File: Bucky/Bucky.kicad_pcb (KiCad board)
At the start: 2 copper layers, 81 x 48 mm, 29 parts, among them J1 XT60PW-M, J10 XT30AW-M, J11 XT30AW-M, J12 XT30AW-M, J13 XT30AW-M, J14 XT30AW-M, J2 XT60PW-M, J3 XT30PW-M, J4 XT30PW-M, J5 XT30PW-M, J6 XT30PW-M, J7 XT30AW-M, J8 XT30AW-M, J9 XT30AW-M

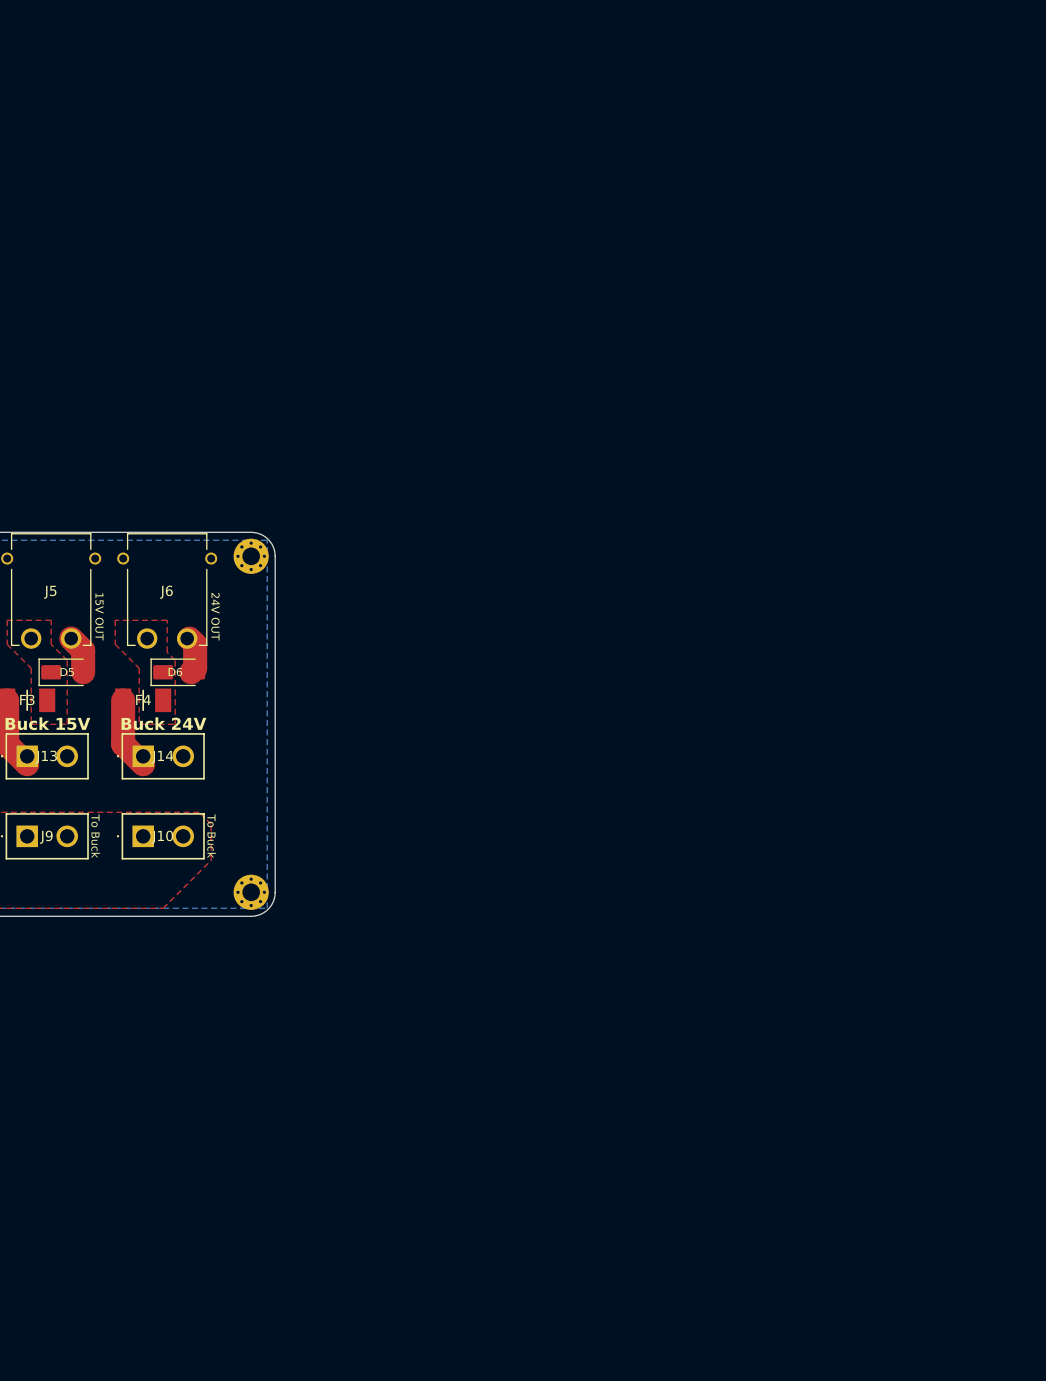
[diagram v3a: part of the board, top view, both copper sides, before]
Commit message: added features from GEODE to the schematics
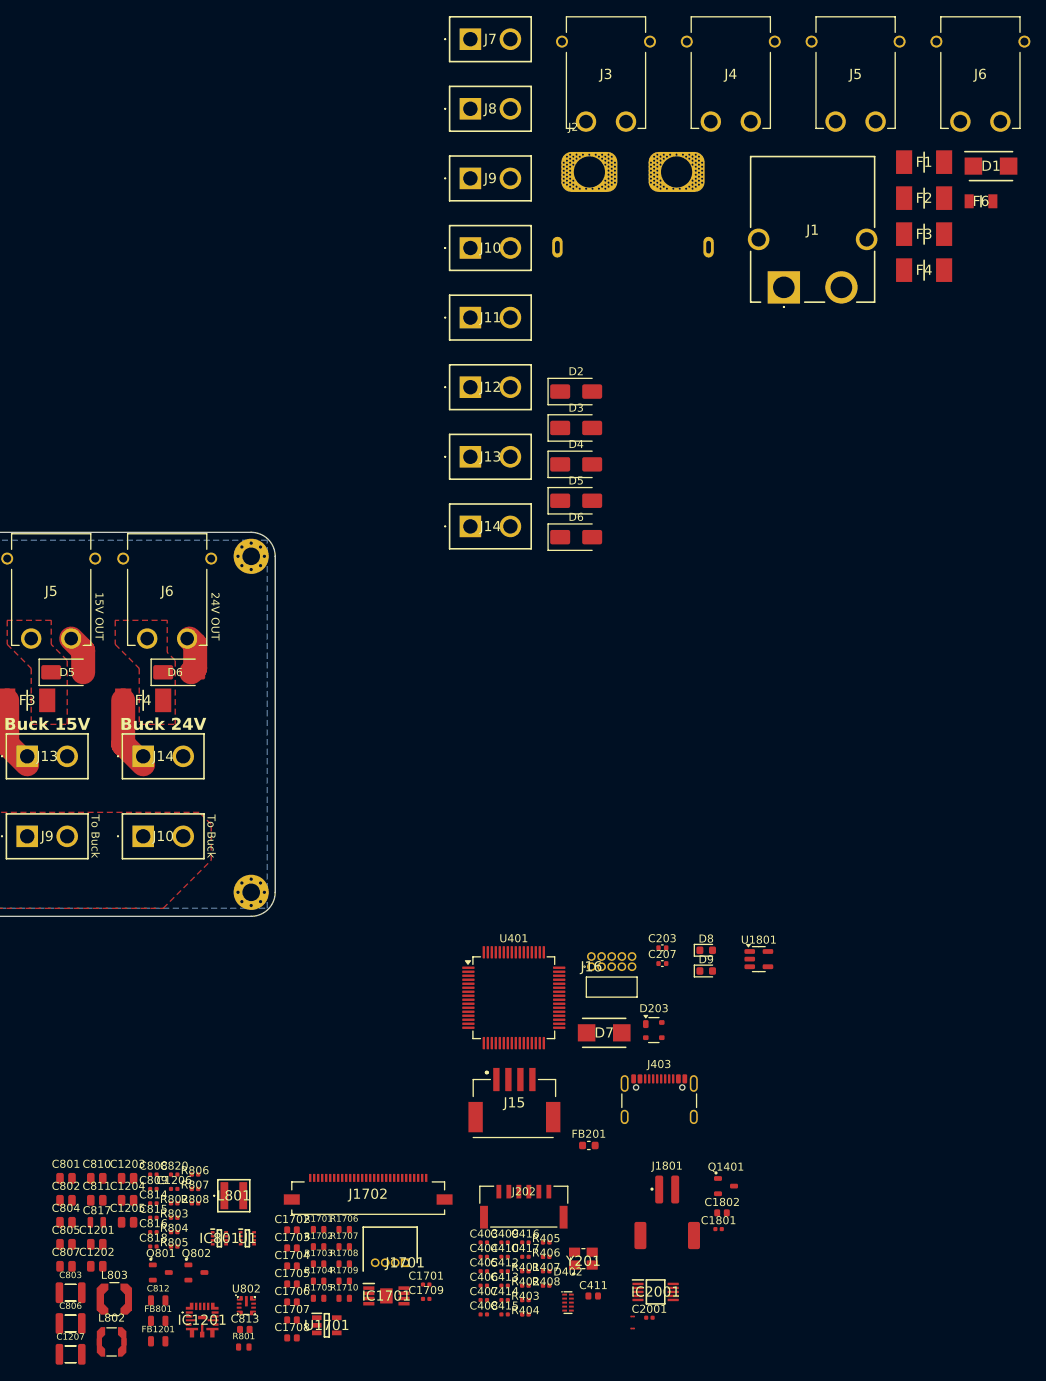
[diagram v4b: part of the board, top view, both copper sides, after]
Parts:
- added C1201: 2u2 X7R 100V, 0_capacitor_smd:C_0805_2012_DensityHigh, F.Cu at (118.7, 155.0)
- added C1202: 2u2 X7R 100V, 0_capacitor_smd:C_0805_2012_DensityHigh, F.Cu at (118.7, 157.8)
- added C1203: 2u2 X7R 100V, 0_capacitor_smd:C_0805_2012_DensityHigh, F.Cu at (122.5, 146.8)
- added C1204: 100n X7R 100V, 0_capacitor_smd:C_0805_2012_DensityHigh, F.Cu at (122.5, 149.5)
- added C1205: 2.2u X7R 25V, 0_capacitor_smd:C_0805_2012_DensityHigh, F.Cu at (122.5, 152.2)
- added C1206: 100n X7R 50V, 0_capacitor_smd:C_0402_1005_DensityHigh, F.Cu at (128.4, 148.1)
- added C1207: 10u X7R 25V, 0_capacitor_smd:C_1210_3225_DensityHigh, F.Cu at (115.4, 168.8)
- added C1701: 100n X7R 50V, 0_capacitor_smd:C_0402_1005_DensityHigh, F.Cu at (159.9, 160.0)
- added C1702: 4.7n X7R 50V, 0_capacitor_smd:C_0603_1608_DensityHigh, F.Cu at (143.1, 153.2)
- added C1703: 4.7n X7R 50V, 0_capacitor_smd:C_0603_1608_DensityHigh, F.Cu at (143.1, 155.4)
- added C1704: 4.7n X7R 50V, 0_capacitor_smd:C_0603_1608_DensityHigh, F.Cu at (143.1, 157.7)
- added C1705: 470n X5R 16V, 0_capacitor_smd:C_0603_1608_DensityHigh, F.Cu at (143.1, 159.9)
- added C1706: 470n X5R 16V, 0_capacitor_smd:C_0603_1608_DensityHigh, F.Cu at (143.1, 162.2)
- added C1707: 220n X7R 10V, 0_capacitor_smd:C_0603_1608_DensityHigh, F.Cu at (143.1, 164.4)
- added C1708: 1u X7R 16V, 0_capacitor_smd:C_0603_1608_DensityHigh, F.Cu at (143.1, 166.7)
- added C1709: 100n X7R 50V, 0_capacitor_smd:C_0402_1005_DensityHigh, F.Cu at (159.9, 161.8)
- added C1801: 100n X7R 50V, 0_capacitor_smd:C_0402_1005_DensityHigh, F.Cu at (196.4, 153.1)
- added C1802: 4.7u X7R 16V, 0_capacitor_smd:C_0603_1608_DensityHigh, F.Cu at (196.8, 151.1)
- added C2001: 100n X7R 50V, 0_capacitor_smd:C_0402_1005_DensityHigh, F.Cu at (187.8, 164.2)
- added C203: 12p NP0 25V, Capacitor_SMD:C_0402_1005Metric, F.Cu at (189.4, 117.9)
- added C207: 12p NP0 25V, Capacitor_SMD:C_0402_1005Metric, F.Cu at (189.4, 119.9)
- added C403: 100n X7R 50V, 0_capacitor_smd:C_0402_1005_DensityHigh, F.Cu at (167.1, 154.8)
- added C404: 100n X7R 50V, 0_capacitor_smd:C_0402_1005_DensityHigh, F.Cu at (167.1, 156.6)
- added C405: 100n X7R 50V, 0_capacitor_smd:C_0402_1005_DensityHigh, F.Cu at (167.1, 158.4)
- added C406: 1u X7R 10V, 0_capacitor_smd:C_0402_1005_DensityHigh, F.Cu at (167.1, 160.2)
- added C407: 100n X7R 50V, 0_capacitor_smd:C_0402_1005_DensityHigh, F.Cu at (167.1, 162.0)
- added C408: 100n X7R 50V, 0_capacitor_smd:C_0402_1005_DensityHigh, F.Cu at (167.1, 163.8)
- added C409: 100n X7R 50V, 0_capacitor_smd:C_0402_1005_DensityHigh, F.Cu at (169.7, 154.8)
- added C410: 100n X7R 50V, 0_capacitor_smd:C_0402_1005_DensityHigh, F.Cu at (169.7, 156.6)
- added C411: 4u7 X7R 16V, 0_capacitor_smd:C_0603_1608_DensityHigh, F.Cu at (180.8, 161.5)
- added C412: 1u X7R 10V, 0_capacitor_smd:C_0402_1005_DensityHigh, F.Cu at (169.7, 158.4)
- added C413: 1u X7R 10V, 0_capacitor_smd:C_0402_1005_DensityHigh, F.Cu at (169.7, 160.2)
- added C414: 100n X7R 50V, 0_capacitor_smd:C_0402_1005_DensityHigh, F.Cu at (169.7, 162.0)
- added C415: 1u X7R 10V, 0_capacitor_smd:C_0402_1005_DensityHigh, F.Cu at (169.7, 163.8)
- added C416: 100n X7R 50V, 0_capacitor_smd:C_0402_1005_DensityHigh, F.Cu at (172.3, 154.8)
- added C417: 100n X7R 50V, 0_capacitor_smd:C_0402_1005_DensityHigh, F.Cu at (172.3, 156.6)
- added C801: 2u2 X7R 100V, 0_capacitor_smd:C_0805_2012_DensityHigh, F.Cu at (114.8, 146.8)
- added C802: 100n X7R 100V, 0_capacitor_smd:C_0805_2012_DensityHigh, F.Cu at (114.8, 149.5)
- added C803: 10u X7R 25V, 0_capacitor_smd:C_1210_3225_DensityHigh, F.Cu at (115.4, 161.1)
- added C804: 2.2u X7R 25V, 0_capacitor_smd:C_0805_2012_DensityHigh, F.Cu at (114.8, 152.2)
- added C805: 2.2u X7R 25V, 0_capacitor_smd:C_0805_2012_DensityHigh, F.Cu at (114.8, 155.0)
- added C806: 4.7uF X7R 25V, 0_capacitor_smd:C_1210_3225_DensityHigh, F.Cu at (115.4, 164.9)
- added C807: 22u X7R 10V, 0_capacitor_smd:C_0805_2012_DensityHigh, F.Cu at (114.8, 157.8)
- added C808: 100n X7R 50V, 0_capacitor_smd:C_0402_1005_DensityHigh, F.Cu at (125.8, 146.3)
- added C809: 100n X7R 50V, 0_capacitor_smd:C_0402_1005_DensityHigh, F.Cu at (125.8, 148.1)
- added C810: 2u2 X7R 100V, 0_capacitor_smd:C_0805_2012_DensityHigh, F.Cu at (118.7, 146.8)
- added C811: 2u2 X7R 100V, 0_capacitor_smd:C_0805_2012_DensityHigh, F.Cu at (118.7, 149.5)
- added C812: 2u2 X7R 100V, 0_resistor_smd:R_0805_2012_DensityHigh, F.Cu at (126.4, 162.0)
- added C813: 100n X7R 100V, 0_capacitor_smd:C_0603_1608_DensityHigh, F.Cu at (137.2, 165.6)
- added C814: 1u X7R 10V, 0_capacitor_smd:C_0402_1005_DensityHigh, F.Cu at (125.8, 149.9)
- added C815: 100n X7R 50V, 0_capacitor_smd:C_0402_1005_DensityHigh, F.Cu at (125.8, 151.7)
- added C816: 100n X7R 50V, 0_capacitor_smd:C_0402_1005_DensityHigh, F.Cu at (125.8, 153.5)
- added C817: 22u X7R 10V, 0_capacitor_smd:C_0805_2012_DensityHighest, F.Cu at (118.7, 152.2)
- added C818: 1u X7R 10V, 0_capacitor_smd:C_0402_1005_DensityHigh, F.Cu at (125.8, 155.3)
- added C820: 1u X7R 10V, 0_capacitor_smd:C_0402_1005_DensityHigh, F.Cu at (128.4, 146.3)
- added D1: SMBJ51CD-M3_H, SamacSys_Parts:DIOM5436X244N, F.Cu at (230.5, 20.2)
- added D2: SMAJ24A, Diode_SMD:D_SMA, F.Cu at (178.6, 48.4)
- added D203: PRTR5V0U2X, Package_TO_SOT_SMD:SOT-143, F.Cu at (188.3, 128.2)
- added D3: SMAJ5.0A, Diode_SMD:D_SMA, F.Cu at (178.6, 53.0)
- added D4: SMAJ12A, Diode_SMD:D_SMA, F.Cu at (178.6, 57.5)
- added D402: PESD4USB3U-TBSX, 0_package_DFN_QFN:SOT1176D, F.Cu at (177.6, 162.3)
- added D5: SMAJ15A, Diode_SMD:D_SMA, F.Cu at (178.6, 62.1)
- added D6: SMAJ24A, Diode_SMD:D_SMA, F.Cu at (178.6, 66.6)
- added D7: SMBJ3V3-M3_5B, SamacSys_Parts:DIONM5436X244N, F.Cu at (182.1, 128.6)
- added D8: GREEN, LED_SMD:LED_0603_1608Metric, F.Cu at (194.9, 118.2)
- added D9: GREEN, LED_SMD:LED_0603_1608Metric, F.Cu at (194.9, 120.8)
- added F1: 0451015.MRL, SamacSys_Parts:FUSC6127X294N, F.Cu at (222.1, 19.7)
- added F2: 0451015.MRL, SamacSys_Parts:FUSC6127X294N, F.Cu at (222.1, 24.2)
- added F3: 0451015.MRL, SamacSys_Parts:FUSC6127X294N, F.Cu at (222.1, 28.7)
- added F4: 0451015.MRL, SamacSys_Parts:FUSC6127X294N, F.Cu at (222.1, 33.2)
- added F6: 0806040.WR, SamacSys_Parts:FUSC3216X110N, F.Cu at (229.2, 24.6)
- added FB1201: 1k @ 100MHz, 0_resistor_smd:R_0805_2012_DensityHigh, F.Cu at (126.4, 167.1)
- added FB201: 100R@100MHz, Inductor_SMD:L_0603_1608Metric, F.Cu at (180.2, 142.6)
- added FB801: 1k @ 100MHz, 0_resistor_smd:R_0805_2012_DensityHigh, F.Cu at (126.4, 164.6)
- added IC1201: MAX25262AFOF_VY+, 0_switching_regulator:MAX25262AFOFVY, F.Cu at (131.9, 164.5)
- added IC1701: TPA6205A1DGN, 0_connectors:SOP65P490X110-9N, F.Cu at (154.9, 161.4)
- added IC2001: INA239AQDGSRQ1, 0_diode_smd:SOP50P490X110-10N, F.Cu at (188.6, 160.9)
- added IC801: TPS629206QDRLRQ1, 0_switching_regulator:SOTFL50P160X60-8N, F.Cu at (134.0, 154.2)
- added J1: XT60PW-M, SamacSys_Parts:XT60PWM, F.Cu at (204.6, 35.4)
- added J10: XT30AW-M, SamacSys_Parts:XT30AWM, F.Cu at (165.4, 30.5)
- added J11: XT30AW-M, SamacSys_Parts:XT30AWM, F.Cu at (165.4, 39.2)
- added J12: XT30AW-M, SamacSys_Parts:XT30AWM, F.Cu at (165.4, 47.9)
- added J13: XT30AW-M, SamacSys_Parts:XT30AWM, F.Cu at (165.4, 56.6)
- added J14: XT30AW-M, SamacSys_Parts:XT30AWM, F.Cu at (165.4, 65.3)
- added J15: 502585-0470, SamacSys_Parts:5025850470, F.Cu at (170.9, 138.0)
- added J16: FTSH-105-01-F-D-RA-K, SamacSys_Parts:FTSH-105-XX-YYY-D-RA-K, F.Cu at (180.5, 120.3)
- added J1701: 53048-0450, 0_connectors:SHDRRA4W35P0X125_1X4_675X550X350P, F.Cu at (157.2, 157.3)
- added J1702: 505110-3091, 0_connectors:5051103091, F.Cu at (152.6, 148.7)
- added J1801: S2B-PH-SM4-TB, 0_connectors:JST_PH_S2B-PH-SM4-TB_1x02-1MP_P2.00mm_Horizontal, F.Cu at (190.0, 151.0)
- added J2: XT90PW-M, 0_connectors:AMASS_XT90PW-M, F.Cu at (185.7, 30.4)
- added J202: Conn_Picoblade_JST_DEBUG, 0_connectors:CONN_SM06B-GHS-TB_JST, F.Cu at (172.1, 150.3)
- added J3: XT30PW-M, SamacSys_Parts:XT30PWM, F.Cu at (182.3, 8.75)
- added J4: XT30PW-M, SamacSys_Parts:XT30PWM, F.Cu at (197.9, 8.75)
- added J403: USB4105-GF-A, Connector_USB:USB_C_Receptacle_GCT_USB4105-xx-A_16P_TopMnt_Horizontal, F.Cu at (189.0, 138.0)
- added J5: XT30PW-M, SamacSys_Parts:XT30PWM, F.Cu at (213.6, 8.75)
- added J6: XT30PW-M, SamacSys_Parts:XT30PWM, F.Cu at (229.2, 8.75)
- added J7: XT30AW-M, SamacSys_Parts:XT30AWM, F.Cu at (165.4, 4.36)
- added J8: XT30AW-M, SamacSys_Parts:XT30AWM, F.Cu at (165.4, 13.1)
- added J9: XT30AW-M, SamacSys_Parts:XT30AWM, F.Cu at (165.4, 21.8)
- added L801: 6u8, 0_inductor_smd:XEL4030682MEC, F.Cu at (135.8, 148.9)
- added L802: 2u2, 0_inductor_smd:L_Coilcraft_LPS3314, F.Cu at (120.5, 167.2)
- added L803: 22u, 0_inductor_smd:L_Coilcraft_LPS4018, F.Cu at (120.9, 161.8)
- added NT1601: NetTieShuntH, 0_net_tie:NetTie-2_SMD_Pad0.2mm, F.Cu at (185.7, 164.0)
- added NT1602: NetTieShuntL, 0_net_tie:NetTie-2_SMD_Pad0.2mm, F.Cu at (185.7, 165.5)
- added Q1401: PMV90ENER, 0_package_SOT_TO_SMD:SOT-23-3, F.Cu at (197.3, 147.7)
- added Q801: PMV90ENER, 0_package_SOT_TO_SMD:SOT-23-3, F.Cu at (126.7, 158.5)
- added Q802: PMV90ENER, 0_package_SOT_TO_SMD:SOT-23-3, F.Cu at (131.2, 158.5)
- added R1701: 33 1% 1/10W, 0_resistor_smd:R_0603_1608_DensityHigh, F.Cu at (146.4, 153.2)
- added R1702: 33 1% 1/10W, 0_resistor_smd:R_0603_1608_DensityHigh, F.Cu at (146.4, 155.3)
- added R1703: 1k 1% 1/10W, 0_resistor_smd:R_0603_1608_DensityHigh, F.Cu at (146.4, 157.4)
- added R1704: 1k 1% 1/10W, 0_resistor_smd:R_0603_1608_DensityHigh, F.Cu at (146.4, 159.6)
- added R1705: 47k 1% 1/10W, 0_resistor_smd:R_0603_1608_DensityHigh, F.Cu at (146.4, 161.8)
- added R1706: 1k 1% 1/10W, 0_resistor_smd:R_0603_1608_DensityHigh, F.Cu at (149.6, 153.2)
- added R1707: 10k 1% 1/10W, 0_resistor_smd:R_0603_1608_DensityHigh, F.Cu at (149.6, 155.3)
- added R1708: 10k 1% 1/10W, 0_resistor_smd:R_0603_1608_DensityHigh, F.Cu at (149.6, 157.4)
- added R1709: 20k 1% 1/10W, 0_resistor_smd:R_0603_1608_DensityHigh, F.Cu at (149.6, 159.6)
- added R1710: 20k 1% 1/10W, 0_resistor_smd:R_0603_1608_DensityHigh, F.Cu at (149.6, 161.8)
- added R401: 33k 1% 1/16W, 0_resistor_smd:R_0402_1005_DensityHigh, F.Cu at (172.3, 158.4)
- added R402: 5.1k 1% 1/16W, 0_resistor_smd:R_0402_1005_DensityHigh, F.Cu at (172.3, 160.2)
- added R403: 5.1k 1% 1/16W, 0_resistor_smd:R_0402_1005_DensityHigh, F.Cu at (172.3, 162.0)
- added R404: 10k 1% 1/16W, 0_resistor_smd:R_0402_1005_DensityHigh, F.Cu at (172.3, 163.8)
- added R405: 10k 1% 1/16W, 0_resistor_smd:R_0402_1005_DensityHigh, F.Cu at (174.9, 154.8)
- added R406: 10k 1% 1/16W, 0_resistor_smd:R_0402_1005_DensityHigh, F.Cu at (174.9, 156.6)
- added R407: 27R 1% 1/5W, 0_resistor_smd:R_0402_1005_DensityHigh, F.Cu at (174.9, 158.4)
- added R408: 27R 1% 1/5W, 0_resistor_smd:R_0402_1005_DensityHigh, F.Cu at (174.9, 160.2)
- added R801: 34k 1% 1/4W, 0_resistor_smd:R_0603_1608_DensityHigh, F.Cu at (137.1, 167.8)
- added R802: 0R, 0_resistor_smd:R_0402_1005_DensityHigh, F.Cu at (128.4, 149.9)
- added R803: 10k 1%, 0_resistor_smd:R_0402_1005_DensityHigh, F.Cu at (128.4, 151.7)
- added R804: 10.7k, 0_resistor_smd:R_0402_1005_DensityHigh, F.Cu at (128.4, 153.5)
- added R805: 37k, 0_resistor_smd:R_0402_1005_DensityHigh, F.Cu at (128.4, 155.3)
- added R806: 10k 1%, 0_resistor_smd:R_0402_1005_DensityHigh, F.Cu at (131.0, 146.3)
- added R807: 470R 1% 1/8W, 0_resistor_smd:R_0402_1005_DensityHigh, F.Cu at (131.0, 148.1)
- added R808: 470R 1% 1/8W, 0_resistor_smd:R_0402_1005_DensityHigh, F.Cu at (131.0, 149.9)
- added U1: TPS2116DRLR, 0_switching_regulator:SOTFL50P160X60-8N, F.Cu at (137.5, 154.2)
- added U1701: 74LVC1G125, 0_package_SON:SOT95P280X145-5N, F.Cu at (147.4, 165.1)
- added U1801: DGD0216WT-7, Package_TO_SOT_SMD:TSOT-23-5, F.Cu at (201.5, 119.3)
- added U401: STM32G483RET6, Package_QFP:LQFP-64_10x10mm_P0.5mm, F.Cu at (170.8, 124.2)
- added U802: LMR36506MSC5RPERQ1, 0_switching_regulator:LMR36503, F.Cu at (137.4, 162.7)
- added Y201: ABM8W-48.0000MHZ-4-D1X-T3, 0_diode_smd:ABM8W480000MHZ6D1XT3, F.Cu at (179.5, 157.1)

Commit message: adapted schematics and added more protection from GEODE (Reverse Current)
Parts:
- removed the D1 at (69.0, 69.0)
- removed the D2 at (73.0, 111.0)
- removed D3 (x2): SMAJ5.0A, Diode_SMD:D_SMA
- removed D4 (x2): SMAJ12A, Diode_SMD:D_SMA
- removed D5 (x2): SMAJ15A, Diode_SMD:D_SMA
- removed D6 (x2): SMAJ24A, Diode_SMD:D_SMA
- removed the F1 at (82.0, 87.0)
- removed the F2 at (96.0, 87.0)
- removed the F3 at (110.0, 87.0)
- removed the F4 at (124.5, 87.0)
- removed the F6 at (75.5, 88.5)
- removed H1, H2, H3, H501: M2 (3.2mm), MountingHole:MountingHole_2.2mm_M2_Pad_Via
- removed the J1 at (71.0, 84.6)
- removed J10 (x2), J9 (x2): XT30AW-M, SamacSys_Parts:XT30AWM
- removed the J11 at (81.0, 94.0)
- removed the J12 at (95.5, 94.0)
- removed the J13 at (110.0, 94.0)
- removed the J14 at (124.5, 94.0)
- removed the J2 at (71.0, 102.6)
- removed the J2 at (185.7, 30.4)
- removed the J3 at (84.0, 73.4)
- removed the J4 at (98.5, 73.4)
- removed the J5 at (113.0, 73.4)
- removed the J6 at (127.5, 73.4)
- removed the J7 at (95.5, 104.0)
- removed the J7 at (165.4, 4.36)
- removed the J8 at (165.4, 13.1)
- removed the J8 at (81.0, 104.0)
- added C1: 100n X7R 50V, 0_capacitor_smd:C_0402_1005_DensityHigh, F.Cu at (98.7, 31.0)
- added C1801: 100n X7R 50V, 0_capacitor_smd:C_0402_1005_DensityHigh, F.Cu at (242.1, 84.5)
- added C1802: 4.7u X7R 16V, 0_capacitor_smd:C_0603_1608_DensityHigh, F.Cu at (238.3, 84.2)
- added C2: 100n X7R 50V, 0_capacitor_smd:C_0402_1005_DensityHigh, F.Cu at (98.7, 32.8)
- added C3: 100n X7R 50V, 0_capacitor_smd:C_0402_1005_DensityHigh, F.Cu at (98.7, 34.6)
- added C4: 10n X7R 100V, 0_capacitor_smd:C_0402_1005_DensityHigh, F.Cu at (186.1, 30.9)
- added C5: 10n X7R 100V, 0_capacitor_smd:C_0402_1005_DensityHigh, F.Cu at (186.1, 32.7)
- added C6: 100n X7R 50V, 0_capacitor_smd:C_0402_1005_DensityHigh, F.Cu at (186.1, 34.5)
- added C7: 100n X7R 50V, 0_capacitor_smd:C_0402_1005_DensityHigh, F.Cu at (186.1, 36.3)
- added C701: 10n X7R 100V, 0_capacitor_smd:C_0402_1005_DensityHigh, F.Cu at (186.1, 38.1)
- added C702: 10n X7R 100V, 0_capacitor_smd:C_0402_1005_DensityHigh, F.Cu at (186.1, 39.9)
- added C703: 100n X7R 50V, 0_capacitor_smd:C_0402_1005_DensityHigh, F.Cu at (186.1, 41.7)
- added C704: 100n X7R 50V, 0_capacitor_smd:C_0402_1005_DensityHigh, F.Cu at (186.1, 43.5)
- added D11: SMAJ15A, Diode_SMD:D_SMA, F.Cu at (90.0, 31.4)
- added D13: SMAJ24A, Diode_SMD:D_SMA, F.Cu at (90.0, 35.9)
- added D702: SMAJ5A, Diode_SMD:D_SMA, F.Cu at (90.0, 40.5)
- added D704: SMAJ12A, Diode_SMD:D_SMA, F.Cu at (90.0, 45.0)
- added IC1: INA239AQDGSRQ1, 0_diode_smd:SOP50P490X110-10N, F.Cu at (65.0, 71.5)
- added IC2: INA239AQDGSRQ1, 0_diode_smd:SOP50P490X110-10N, F.Cu at (81.0, 71.5)
- added IC3: INA239AQDGSRQ1, 0_diode_smd:SOP50P490X110-10N, F.Cu at (95.5, 71.5)
- added IC4: LTC4372CMS8#TRPBF, 0_package_SOT_TO_SMD:SOP65P490X110-8N, F.Cu at (95.0, 58.0)
- added IC5: LTC4372CMS8#TRPBF, 0_package_SOT_TO_SMD:SOP65P490X110-8N, F.Cu at (111.5, 57.5)
- added IC701: LTC4372CMS8#TRPBF, 0_package_SOT_TO_SMD:SOP65P490X110-8N, F.Cu at (62.7, 57.2)
- added IC702: LTC4372CMS8#TRPBF, 0_package_SOT_TO_SMD:SOP65P490X110-8N, F.Cu at (78.7, 58.0)
- added J17: XT30UPB-F, SamacSys_Parts:XT30UPBF, B.Cu at (92.2, 102.0)
- added J18: XT30UPB-F, SamacSys_Parts:XT30UPBF, B.Cu at (83.9, 102.0)
- added J1801: S2B-PH-SM4-TB, 0_connectors:JST_PH_S2B-PH-SM4-TB_1x02-1MP_P2.00mm_Horizontal, F.Cu at (210.0, 157.5)
- added J2: XT60PW-F, SamacSys_Parts:XT60PWF, B.Cu at (47.7, 68.2)
- added J7: XT30UPB-F, SamacSys_Parts:XT30UPBF, B.Cu at (108.8, 102.0)
- added J8: XT30UPB-F, SamacSys_Parts:XT30UPBF, B.Cu at (100.5, 102.0)
- added NT1: NetTieShuntH, 0_net_tie:NetTie-2_SMD_Pad0.2mm, F.Cu at (83.7, 74.5)
- added NT2: NetTieShuntL, 0_net_tie:NetTie-2_SMD_Pad0.2mm, F.Cu at (83.7, 76.0)
- added NT3: NetTieShuntH, 0_net_tie:NetTie-2_SMD_Pad0.2mm, F.Cu at (92.7, 74.5)
- added NT4: NetTieShuntL, 0_net_tie:NetTie-2_SMD_Pad0.2mm, F.Cu at (92.7, 76.0)
- added NT5: NetTieShuntH, 0_net_tie:NetTie-2_SMD_Pad0.2mm, F.Cu at (113.2, 74.5)
- added NT6: NetTieShuntL, 0_net_tie:NetTie-2_SMD_Pad0.2mm, F.Cu at (113.2, 76.0)
- added Q1: BSC016N06NSATMA1, 0_transistor_fet:PG-TDSON-8_INF, F.Cu at (102.5, 58.0)
- added Q1401: PMV90ENER, 0_package_SOT_TO_SMD:SOT-23-3, F.Cu at (238.8, 80.8)
- added Q2: BSC016N06NSATMA1, 0_transistor_fet:PG-TDSON-8_INF, F.Cu at (118.5, 58.0)
- added Q3: BSC016N06NSATMA1, 0_transistor_fet:PG-TDSON-8_INF, F.Cu at (99.3, 52.0)
- added Q4: BSC016N06NSATMA1, 0_transistor_fet:PG-TDSON-8_INF, F.Cu at (115.5, 52.0)
- added Q701: BSC016N06NSATMA1, 0_transistor_fet:PG-TDSON-8_INF, F.Cu at (70.8, 58.0)
- added Q702: BSC016N06NSATMA1, 0_transistor_fet:PG-TDSON-8_INF, F.Cu at (86.8, 58.6)
- added Q703: BSC016N06NSATMA1, 0_transistor_fet:PG-TDSON-8_INF, F.Cu at (67.8, 52.0)
- added Q704: BSC016N06NSATMA1, 0_transistor_fet:PG-TDSON-8_INF, F.Cu at (84.0, 52.0)
- added R1: 0.3m, 0_resistor_smd:RES_WSLP3921_.003OHM_VIS, F.Cu at (103.0, 71.5)
- added R1505: 0.3m, 0_resistor_smd:RES_WSLP3921_.003OHM_VIS, F.Cu at (72.0, 71.5)
- added R2: 0.3m, 0_resistor_smd:RES_WSLP3921_.003OHM_VIS, F.Cu at (88.0, 72.0)
- added R3: 0.3m, 0_resistor_smd:RES_WSLP3921_.003OHM_VIS, F.Cu at (119.0, 71.5)
- added R4: 10R 1% 1/8W, 0_resistor_smd:R_0805_2012_DensityHigh, F.Cu at (168.1, 56.4)
- added R5: 10R 1% 1/8W, 0_resistor_smd:R_0805_2012_DensityHigh, F.Cu at (168.1, 59.0)
- added R6: 1k 1% 1/10W, 0_resistor_smd:R_0603_1608_DensityHigh, F.Cu at (171.6, 56.2)
- added R7: 1k 1% 1/10W, 0_resistor_smd:R_0603_1608_DensityHigh, F.Cu at (171.6, 58.4)
- added R701: 10R 1% 1/8W, 0_resistor_smd:R_0805_2012_DensityHigh, F.Cu at (168.1, 61.5)
- added R702: 10R 1% 1/8W, 0_resistor_smd:R_0805_2012_DensityHigh, F.Cu at (168.1, 64.1)
- added R703: 1k 1% 1/10W, 0_resistor_smd:R_0603_1608_DensityHigh, F.Cu at (171.6, 60.5)
- added R704: 1k 1% 1/10W, 0_resistor_smd:R_0603_1608_DensityHigh, F.Cu at (171.6, 62.7)
- added U1801: DGD0216WT-7, Package_TO_SOT_SMD:TSOT-23-5, F.Cu at (239.1, 76.2)
- J1, J11, J12, J13, J14, J15, J16, J1702, J3, J4, J403, J5, J6: moved to B.Cu
- moved D1 191.8 mm to (42.5, 58.5)
- moved F6 182.8 mm to (49.6, 58.6), turned to -90 degrees
- moved F4 182.0 mm to (41.0, 51.5), turned to -90 degrees
- moved F3 178.1 mm to (45.5, 51.5), turned to -90 degrees
- moved F2 174.3 mm to (50.0, 51.5), turned to -90 degrees
- moved F1 170.6 mm to (54.5, 51.5), turned to -90 degrees
- moved J1 164.5 mm to (48.7, 87.9), turned to -90 degrees
- moved C2001 148.6 mm to (99.0, 45.0)
- moved NT1601 147.9 mm to (67.2, 75.5)
- moved NT1602 147.9 mm to (67.2, 77.0)
- moved J3 124.1 mm to (68.0, 57.1), turned to 180 degrees
- moved J5 123.7 mm to (99.6, 57.0), turned to 180 degrees
- moved J4 123.7 mm to (84.0, 57.0), turned to 180 degrees
- moved J6 123.5 mm to (115.5, 57.1), turned to 180 degrees
- moved IC2001 118.0 mm to (111.0, 72.0)
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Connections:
- net /MCU/MA_SHDN_VB renamed /MCU/MV24_SHDN
- net /MCU/MB_SHDN_VB renamed /MCU/MV5_SHDN
- net /MCU/RUN1_A renamed /MCU/MV12_SHDN
- net /MCU/~{FAULT0}_A renamed /MCU/MV15_SHDN
- C1201 pad 1: /PowerGeneration/+VBAT -> /PConnectors/VBuck_in
- C810 pad 1: /PowerGeneration/+VBAT -> /PConnectors/VBuck_in
- FB1201 pad 1: /PowerGeneration/+VBAT -> /PConnectors/VBuck_in
- FB801 pad 1: /PowerGeneration/+VBAT -> /PConnectors/VBuck_in
- J11 pad 1: Net-(F1-Pad2) -> /PConnectors/Vin_5V
- J12 pad 1: Net-(F2-Pad2) -> /PConnectors/Vin_12V
- J13 pad 1: Net-(F3-Pad2) -> /PConnectors/Vin_15V
- J14 pad 1: Net-(F4-Pad2) -> /PConnectors/Vin_24V
- NT1601 pad 2: /Sensor/In -> /PConnectors/Vin_5V
- NT1602 pad 2: /Sensor/Out -> /PConnectors/Vout5V
- U401 pad 10: /MCU/SYNC1 -> unconnected-(U401A-PC2-Pad10)
- U401 pad 11: /MCU/RUN0_B -> unconnected-(U401A-PC3-Pad11)
- U401 pad 12: /MCU/~{FAULT1}_B -> unconnected-(U401A-PA0-Pad12)
- U401 pad 13: /MCU/MB_SHDN_VA -> unconnected-(U401A-PA1-Pad13)
- U401 pad 14: /MCU/~{ALERT}_B -> unconnected-(U401A-PA2-Pad14)
- U401 pad 2: /MCU/LED_CAT1 -> unconnected-(U401A-PC13-Pad2)
- U401 pad 22: /MCU/~{FAULT0}_B -> unconnected-(U401A-PC4-Pad22)
- U401 pad 25: /MCU/FAN_CTRL -> /DisplayInterface/FAN
- U401 pad 26: /MCU/MA_SHDN_VA -> unconnected-(U401A-PB2-Pad26)
- U401 pad 3: /MCU/LED_CAT2 -> unconnected-(U401A-PC14-Pad3)
- U401 pad 30: /MCU/~{FAULT1}_A -> unconnected-(U401A-PB10-Pad30)
- U401 pad 38: /MCU/RUN0_A -> unconnected-(U401A-PC6-Pad38)
- U401 pad 4: /MCU/RUN1_B -> unconnected-(U401A-PC15-Pad4)
- U401 pad 40: /MCU/I2C3_SCL -> unconnected-(U401A-PC8-Pad40)
- U401 pad 41: /MCU/I2C3_SDA -> unconnected-(U401A-PC9-Pad41)
- U401 pad 51: /MCU/SPI3_NSS -> unconnected-(U401A-PA15-Pad51)
- U401 pad 52: /MCU/SPI3_SCK -> unconnected-(U401A-PC10-Pad52)
- U401 pad 53: /MCU/SPI3_MISO -> unconnected-(U401A-PC11-Pad53)
- U401 pad 54: /MCU/SPI3_MOSI -> unconnected-(U401A-PC12-Pad54)
- U401 pad 55: /MCU/~{ALERT}_A -> unconnected-(U401A-PD2-Pad55)
- U401 pad 58: /MCU/FDCAN2_RX -> unconnected-(U401A-PB5-Pad58)
- U401 pad 59: /MCU/FDCAN2_TX -> unconnected-(U401A-PB6-Pad59)
- U401 pad 8: /MCU/IRQ -> unconnected-(U401A-PC0-Pad8)
- U401 pad 9: /MCU/SYNC0 -> unconnected-(U401A-PC1-Pad9)
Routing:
- net GND: track 19.5 -> 0.00 mm
- net Net-(F4-Pad2): track 9.04 -> 0.00 mm
- net Net-(F3-Pad2): track 9.04 -> 0.00 mm
- net Net-(F2-Pad2): track 8.83 -> 0.00 mm
- net Net-(F1-Pad2): track 8.62 -> 0.00 mm
- removed copper zone on F.Cu, net /VBatt_in
- removed copper zone on F.Cu, net /VBuck_in
- removed copper zone on F.Cu, net /Vout_12V
- removed copper zone on F.Cu, net /Vout_15V
- removed copper zone on F.Cu, net /Vout_24V
- removed copper zone on F.Cu, net /Vout_5V
- removed copper zone on B.Cu, net GND
- removed copper zone on F.Cu, net GND
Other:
- board size 81 x 48 mm -> 120.5 x 66 mm
- board text removed: "12V OUT"
- board text removed: "15V OUT"
- board text removed: "24V OUT"
- board text removed: "5V OUT"
- board text removed: "Batt IN"
- board text removed: "Buck 12V"
- board text removed: "Buck 15V"
- board text removed: "Buck 24V"
- board text removed: "Buck 5V"
- board text removed: "Mot OUT"
- board text removed: "To Buck"
